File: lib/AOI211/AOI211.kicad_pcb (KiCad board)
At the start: 2 copper layers, 8 parts

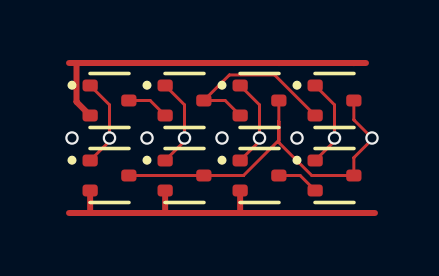
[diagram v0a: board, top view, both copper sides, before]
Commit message: High-density layout with pitch of 1.1mm, which gains 23% !!
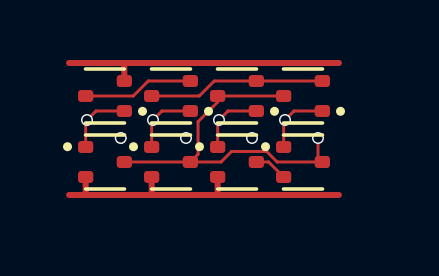
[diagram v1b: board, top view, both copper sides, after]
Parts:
- moved N4 1.14 mm to (7.70, 3.30)
- moved P4 1.06 mm to (7.70, 1.10), turned to 180 degrees
- moved N3 0.87 mm to (5.50, 3.30)
- moved P3 0.76 mm to (5.50, 1.10), turned to 180 degrees
- moved N2 0.64 mm to (3.30, 3.30)
- moved N1 0.47 mm to (1.10, 3.30)
- moved P2 0.47 mm to (3.30, 1.10), turned to 180 degrees
- moved P1 0.21 mm to (1.10, 1.10), turned to 180 degrees
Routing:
- net VDD: track 12.3 -> 9.61 mm
- net intPA: track 1.42 -> 3.70 mm
- net GND: track 12.4 -> 10.8 mm
- net Y: track 13.5 -> 12.5 mm
- net B: track 3.03 -> 2.29 mm
- net C1: track 3.03 -> 2.29 mm
- net A: track 3.03 -> 2.29 mm
- net C2: track 3.03 -> 2.29 mm
- net (no net): vias 4 -> 3

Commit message: All cells now use 1mm*4mm grid rather than 1.1mm*4.4mm
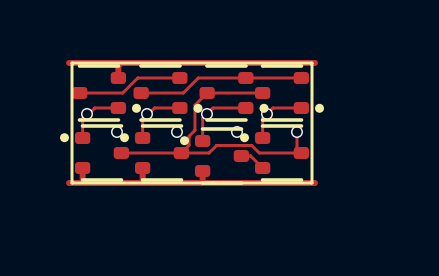
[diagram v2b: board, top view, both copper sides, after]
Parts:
- moved N4 0.76 mm to (7.00, 3.00)
- moved P4 0.71 mm to (7.00, 1.00)
- moved N3 0.54 mm to (5.00, 3.10)
- moved N2 0.42 mm to (3.00, 3.00)
- moved P2 0.36 mm to (2.95, 1.00)
- moved P3 0.36 mm to (5.15, 1.00)
- moved N1 0.32 mm to (1.00, 3.00)
- moved P1 0.22 mm to (0.90, 1.00)
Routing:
- net Y: track 12.5 -> 11.2 mm
- net GND: track 10.8 -> 9.63 mm
- net VDD: track 9.61 -> 8.74 mm

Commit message: Make the pads of my SOT523 footprint very slightly smaller, which is enough to route all the cells and leave the mosfets exactly on the grid
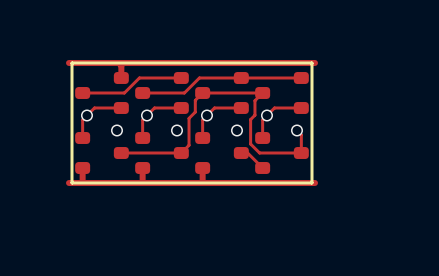
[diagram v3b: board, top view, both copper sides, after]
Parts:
- N1, N2, N3, N4, P1, P2, P3, P4: footprint Package_TO_SOT_SMD:SOT-523 -> RV523:SOT523
- moved P3 0.15 mm to (5.00, 1.00)
- moved N3 0.10 mm to (5.00, 3.00)
- moved P1 0.10 mm to (1.00, 1.00)

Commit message: Propagate MOSFET values to the cells' PCBs
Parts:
- N1, N2, N3, N4: value (none) -> NMOS
- P1, P2, P3, P4: value (none) -> PMOS
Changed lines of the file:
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@@
 			)
 		)
-		(property "Value" ""
+		(property "Value" "NMOS"
 			(at 0 0 0)
 			(layer "F.Fab")
@@
 			)
 		)
-		(property "Value" ""
+		(property "Value" "PMOS"
 			(at 0 0 180)
 			(layer "F.Fab")
@@
 			)
 		)
-		(property "Value" ""
+		(property "Value" "PMOS"
 			(at 0 0 180)
 			(layer "F.Fab")
@@
 			)
 		)
-		(property "Value" ""
+		(property "Value" "NMOS"
 			(at 0 0 0)
 			(layer "F.Fab")
@@
 			)
 		)
-		(property "Value" ""
+		(property "Value" "PMOS"
 			(at 0 0 180)
 			(layer "F.Fab")
@@
 			)
 		)
-		(property "Value" ""
+		(property "Value" "NMOS"
 			(at 0 0 0)
 			(layer "F.Fab")
@@
 			)
 		)
-		(property "Value" ""
+		(property "Value" "PMOS"
 			(at 0 0 180)
 			(layer "F.Fab")
@@
 			)
 		)
-		(property "Value" ""
+		(property "Value" "NMOS"
 			(at 0 0 0)
 			(layer "F.Fab")
